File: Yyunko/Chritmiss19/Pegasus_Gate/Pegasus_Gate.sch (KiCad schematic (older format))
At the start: 19 parts, among them U1 WS2811, U2 WS2811, U3 WS2811, U4 WS2811

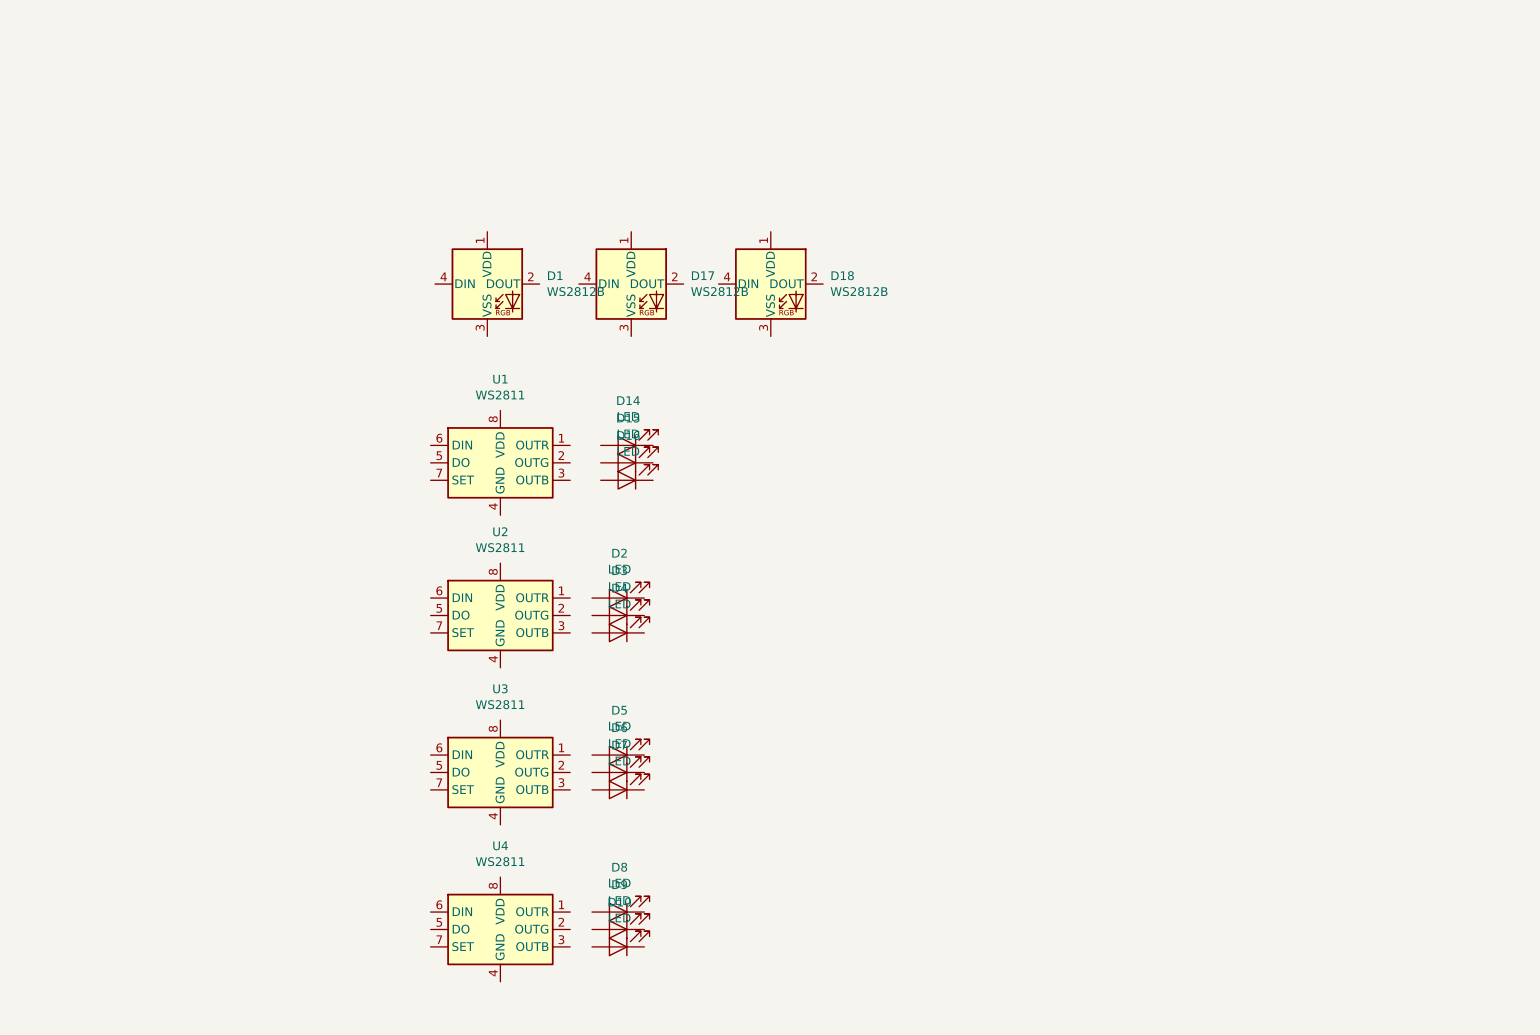
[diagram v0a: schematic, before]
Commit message: Added sidemount LED footprint
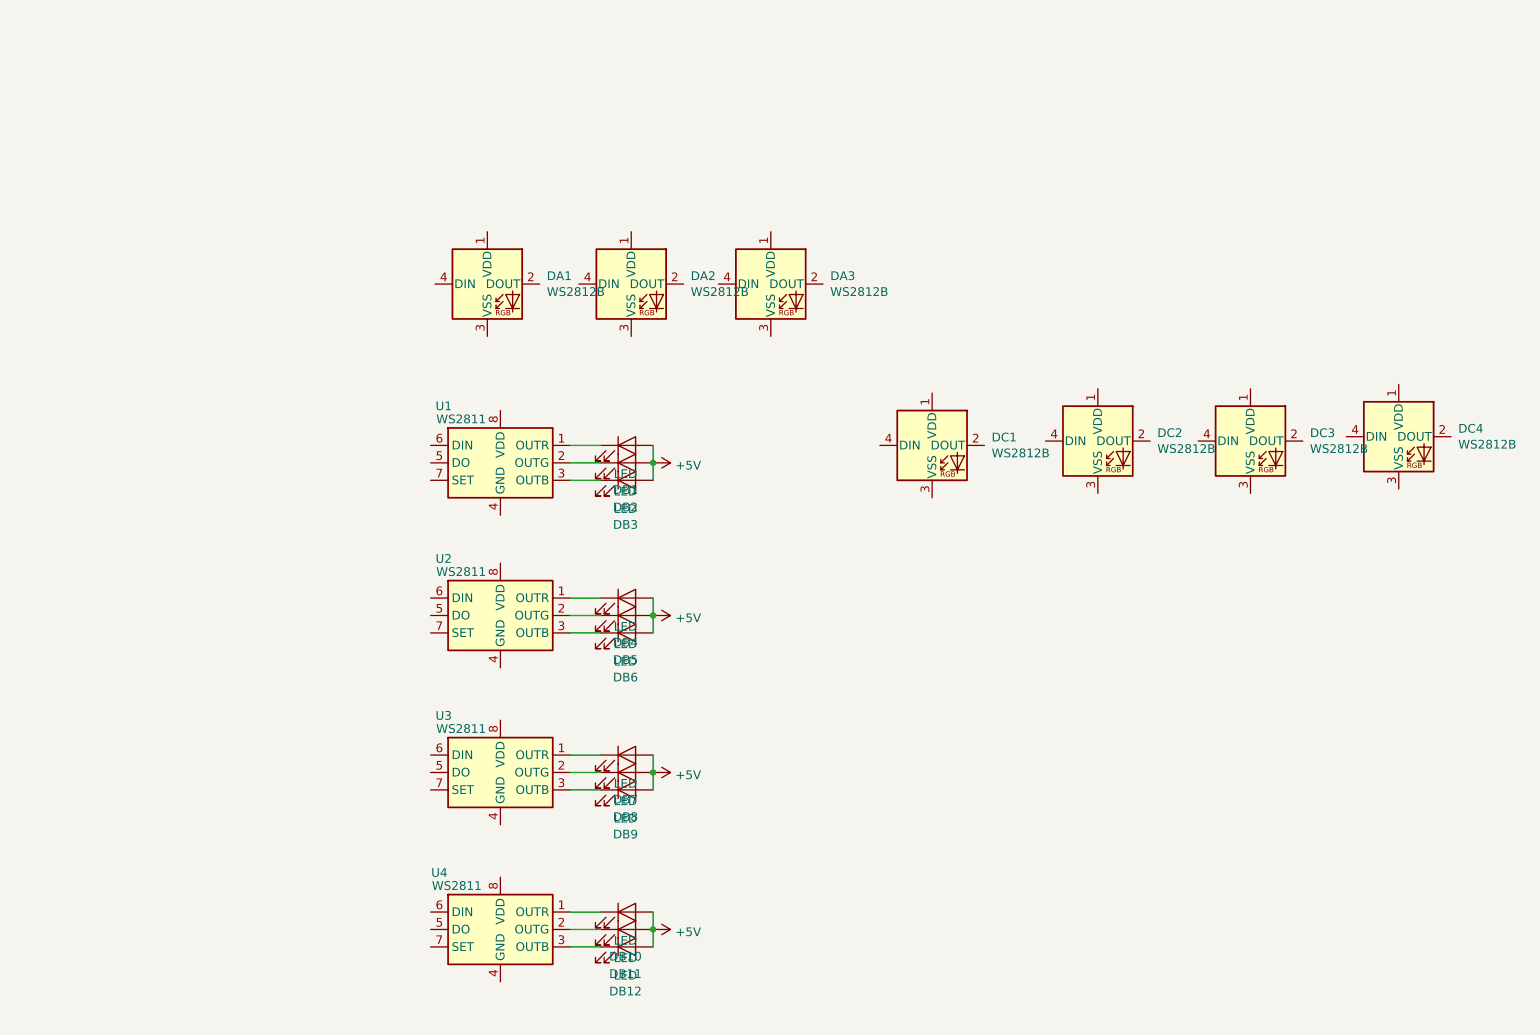
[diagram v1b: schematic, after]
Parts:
- removed D10, D15, D16, D2, D3, D4, D5, D6, D7, D8, D9: LED, LED_SMD:LED_0805_2012Metric_Castellated, symbol Device:LED
- added DB1, DB10, DB11, DB12, DB2, DB4, DB5, DB6, DB7, DB8, DB9: LED, LED_SMD:LED_0805_2012Metric_Castellated, symbol Device:LED
- added DC1, DC2, DC3, DC4: WS2812B, Local:IN-PI42TAS, symbol LED:WS2812B
- U2, U3, U4: footprint (none) -> Package_SO:SSOP-8_3.95x5.21x3.27mm_P1.27mm
- renumbered D1 to DA1, D17 to DA2, D18 to DA3, D14 to DB3
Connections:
- net at U1.1 (OUTR): now also DB1.1 (K)
- net at U1.2 (OUTG): now also DB2.1 (K)
- net at U1.3 (OUTB): now also DB3.1 (K)
- net at U2.1 (OUTR): now also DB4.1 (K)
- net at U2.2 (OUTG): now also DB5.1 (K)
- net at U2.3 (OUTB): now also DB6.1 (K)
- net at U3.1 (OUTR): now also DB7.1 (K)
- net at U3.2 (OUTG): now also DB8.1 (K)
- net at U3.3 (OUTB): now also DB9.1 (K)
- net at U4.1 (OUTR): now also DB10.1 (K)
- net at U4.2 (OUTG): now also DB11.1 (K)
- net at U4.3 (OUTB): now also DB12.1 (K)
- net +5V: now reaches DB3.2 (A)
- net +5V: now also DB1.2 (A), DB10.2 (A), DB11.2 (A), DB12.2 (A), DB2.2 (A), DB4.2 (A), DB5.2 (A), DB6.2 (A), DB7.2 (A), DB8.2 (A), DB9.2 (A)
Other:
- moved on the sheet: DB3

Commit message: Almost sorted all secs out
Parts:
- added C1, C3, C5, C7: 10uF, Capacitor_SMD:C_0805_2012Metric, symbol Device:C
- added C2, C4, C6, C8: 100nF, Capacitor_SMD:C_0805_2012Metric, symbol Device:C_Small
- added DD1, DD2, DD3: WS2812B, Local:IN-PI42TAS, symbol LED:WS2812B
- added J? (x2): Conn_01x03_Female, Connector_PinHeader_2.00mm:PinHeader_1x03_P2.00mm_Vertical, symbol Connector:Conn_01x03_Female
- added JP?: Jumper_NC_Small, Jumper:SolderJumper-2_P1.3mm_Bridged_Pad1.0x1.5mm, symbol Device:Jumper_NC_Small
- renumbered U4 to U1, U3 to U2, U2 to U3, U1 to U4
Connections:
- net +5V: now also DA1.1 (VDD), DA2.1 (VDD), DA3.1 (VDD), U1.8 (VDD), U2.8 (VDD), U3.8 (VDD), U4.8 (VDD), C1.1, C2.1, C3.1, C4.1, C5.1, C6.1, C7.1, C8.1, DD1.1 (VDD), DD2.1 (VDD), DD3.1 (VDD), J?.3 (Pin_3)
- net at DA1.2 (DOUT): now also DD1.4 (DIN)
- net GND: now reaches DA1.3 (VSS)
- net GND: now also DA2.3 (VSS), DA3.3 (VSS), U1.4 (GND), U2.4 (GND), U3.4 (GND), U4.4 (GND), C1.2, C2.2, C3.2, C4.2, C5.2, C6.2, C7.2, C8.2, DD1.3 (VSS), DD2.3 (VSS), DD3.3 (VSS), J?.1 (Pin_1)
- net IN_A: now reaches DA1.4 (DIN)
- net IN_A: now also JP?.2
- net at DA2.2 (DOUT): now also DD2.4 (DIN)
- net at DA2.4 (DIN): now also DD1.2 (DOUT)
- net at DA3.2 (DOUT): now also DD3.4 (DIN)
- net at DA3.4 (DIN): now also DD2.2 (DOUT)
- net IN_C: now reaches U4.5 (DO)
- net IN_C: now also DC1.4 (DIN)
- net at U4.6 (DIN): now also U3.5 (DO)
- net at U3.6 (DIN): now also U2.5 (DO)
- net at U2.6 (DIN): now also U1.5 (DO)
- net IN_B: now reaches U1.6 (DIN)
- net IN_B: now also DD3.2 (DOUT)
- net at DC1.2 (DOUT): now also DC2.4 (DIN)
- net at DC2.2 (DOUT): now also DC3.4 (DIN)
- net at DC3.2 (DOUT): now also DC4.4 (DIN)
- net SIG_OUT: now reaches DC4.2 (DOUT)
- net SIG_OUT: now also J?.2 (Pin_2)
- new net: J?.2 (Pin_2), JP?.1
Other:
- moved on the sheet: DA1, DA2, DA3, DC1, DC2, DC3, DC4

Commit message: Continue woork
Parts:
- gave numbers to parts that had none: 3
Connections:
- net +5V: now also DC1.1 (VDD), DC2.1 (VDD), DC3.1 (VDD), DC4.1 (VDD), J2.1 (Pin_1)
- net GND: now also DC1.3 (VSS), DC2.3 (VSS), DC3.3 (VSS), DC4.3 (VSS), J2.3 (Pin_3)
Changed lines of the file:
@@
 	8750 4475 8925 4475
 $Comp
-L Connector:Conn_01x03_Female J?
+L Connector:Conn_01x03_Female J1
 U 1 1 5DE0950A
 P 3400 2375
-F 0 "J?" H 3294 2050 50  0000 C CNN
+F 0 "J1" H 3294 2050 50  0000 C CNN
 F 1 "Conn_01x03_Female" H 3294 2141 50  0000 C CNN
 F 2 "Connector_PinHeader_2.00mm:PinHeader_1x03_P2.00mm_Vertical" H 3400 2375 50  0001 C CNN
@@
 $EndComp
 $Comp
-L Connector:Conn_01x03_Female J?
+L Connector:Conn_01x03_Female J2
 U 1 1 5DE0969D
 P 10275 2325
-F 0 "J?" H 10169 2000 50  0000 C CNN
+F 0 "J2" H 10169 2000 50  0000 C CNN
 F 1 "Conn_01x03_Female" H 10169 2091 50  0000 C CNN
 F 2 "Connector_PinHeader_2.00mm:PinHeader_1x03_P2.00mm_Vertical" H 10275 2325 50  0001 C CNN
@@
 $EndComp
 $Comp
-L power:GND #PWR?
+L power:GND #PWR0122
 U 1 1 5DE0CA89
 P 3675 2525
-F 0 "#PWR?" H 3675 2275 50  0001 C CNN
+F 0 "#PWR0122" H 3675 2275 50  0001 C CNN
 F 1 "GND" H 3680 2352 50  0000 C CNN
 F 2 "" H 3675 2525 50  0001 C CNN
@@
 	3950 2275 3950 2100
 $Comp
-L power:+5V #PWR?
+L power:+5V #PWR0123
 U 1 1 5DE11560
 P 3950 2100
-F 0 "#PWR?" H 3950 1950 50  0001 C CNN
+F 0 "#PWR0123" H 3950 1950 50  0001 C CNN
 F 1 "+5V" H 3965 2273 50  0000 C CNN
 F 2 "" H 3950 2100 50  0001 C CNN
@@
 $EndComp
 $Comp
-L Device:Jumper_NC_Small JP?
+L Device:Jumper_NC_Small JP1
 U 1 1 5DE11BC5
 P 3750 2375
-F 0 "JP?" H 3750 2587 50  0000 C CNN
+F 0 "JP1" H 3750 2587 50  0000 C CNN
 F 1 "Jumper_NC_Small" H 3750 2496 50  0000 C CNN
 F 2 "Jumper:SolderJumper-2_P1.3mm_Bridged_Pad1.0x1.5mm" H 3750 2375 50  0001 C CNN
@@
 Text Label 10925 2325 2    50   ~ 0
 SIG_OUT
+Wire Wire Line
+	7050 2925 8025 2925
+Wire Wire Line
+	8025 2925 8550 2925
+Connection ~ 8025 2925
+Wire Wire Line
+	9025 2925 10025 2925
+Connection ~ 9025 2925
+Wire Wire Line
+	10025 3525 9025 3525
+Wire Wire Line
+	9025 3525 8550 3525
+Connection ~ 9025 3525
+Wire Wire Line
+	8025 3525 7050 3525
+Connection ~ 8025 3525
+$Comp
+L power:+5V #PWR0124
+U 1 1 5DDFCAF7
+P 8550 2925
+F 0 "#PWR0124" H 8550 2775 50  0001 C CNN
+F 1 "+5V" H 8565 3098 50  0000 C CNN
+F 2 "" H 8550 2925 50  0001 C CNN
+F 3 "" H 8550 2925 50  0001 C CNN
+	1    8550 2925
+	1    0    0    -1
+$EndComp
+Connection ~ 8550 2925
+Wire Wire Line
+	8550 2925 9025 2925
+$Comp
+L power:GND #PWR0125
+U 1 1 5DDFCBC9
+P 8550 3525
+F 0 "#PWR0125" H 8550 3275 50  0001 C CNN
+F 1 "GND" H 8555 3352 50  0000 C CNN
+F 2 "" H 8550 3525 50  0001 C CNN
+F 3 "" H 8550 3525 50  0001 C CNN
+	1    8550 3525
+	1    0    0    -1
+$EndComp
+Connection ~ 8550 3525
+Wire Wire Line
+	8550 3525 8025 3525
+$Comp
+L power:GND #PWR0126
+U 1 1 5DDFD954
+P 10625 2175
+F 0 "#PWR0126" H 10625 1925 50  0001 C CNN
+F 1 "GND" V 10630 2047 50  0000 R CNN
+F 2 "" H 10625 2175 50  0001 C CNN
+F 3 "" H 10625 2175 50  0001 C CNN
+	1    10625 2175
+	0    -1   -1   0
+$EndComp
+$Comp
+L power:+5V #PWR0127
+U 1 1 5DDFDA93
+P 10650 2450
+F 0 "#PWR0127" H 10650 2300 50  0001 C CNN
+F 1 "+5V" V 10665 2578 50  0000 L CNN
+F 2 "" H 10650 2450 50  0001 C CNN
+F 3 "" H 10650 2450 50  0001 C CNN
+	1    10650 2450
+	0    1    1    0
+$EndComp
+Wire Wire Line
+	10475 2425 10650 2425
+Wire Wire Line
+	10650 2425 10650 2450
+Wire Wire Line
+	10475 2225 10625 2225
+Wire Wire Line
+	10625 2225 10625 2175
 $EndSCHEMATC

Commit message: Begin work on assigning part nums
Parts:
- DA1, DA2, DA3: value WS2812B -> BL-HRGB32K-3-TRBCT-ND
- DB1, DB10, DB11, DB12, DB2, DB3, DB4, DB5, DB6, DB7, DB8, DB9: value LED -> 754-1437-6-ND
- DC1, DC2, DC3, DC4, DD1, DD2, DD3: value WS2812B -> 1830-1206-1-ND
- U4: value WS2811 -> 1528-1537-ND
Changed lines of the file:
@@
 P 5075 1550
 F 0 "DA1" H 5416 1596 50  0000 L CNN
-F 1 "WS2812B" H 5416 1505 50  0000 L CNN
+F 1 "BL-HRGB32K-3-TRBCT-ND" H 5416 1505 50  0000 L CNN
 F 2 "LED_SMD:LED_WS2812B_PLCC4_5.0x5.0mm_P3.2mm" H 5125 1250 50  0001 L TNN
 F 3 "https://cdn-shop.adafruit.com/datasheets/WS2812B.pdf" H 5175 1175 50  0001 L TNN
@@
 P 6400 1675
 F 0 "DA2" H 6741 1721 50  0000 L CNN
-F 1 "WS2812B" H 6741 1630 50  0000 L CNN
+F 1 "BL-HRGB32K-3-TRBCT-ND" H 6741 1630 50  0000 L CNN
 F 2 "LED_SMD:LED_WS2812B_PLCC4_5.0x5.0mm_P3.2mm" H 6450 1375 50  0001 L TNN
 F 3 "https://cdn-shop.adafruit.com/datasheets/WS2812B.pdf" H 6500 1300 50  0001 L TNN
@@
 P 7750 1550
 F 0 "DA3" H 8091 1596 50  0000 L CNN
-F 1 "WS2812B" H 8091 1505 50  0000 L CNN
+F 1 "BL-HRGB32K-3-TRBCT-ND" H 8091 1505 50  0000 L CNN
 F 2 "LED_SMD:LED_WS2812B_PLCC4_5.0x5.0mm_P3.2mm" H 7800 1250 50  0001 L TNN
 F 3 "https://cdn-shop.adafruit.com/datasheets/WS2812B.pdf" H 7850 1175 50  0001 L TNN
@@
 P 5375 3600
 F 0 "U4" H 5050 3925 50  0000 C CNN
-F 1 "WS2811" H 5150 3850 50  0000 C CNN
+F 1 "1528-1537-ND" H 5150 3850 50  0000 C CNN
 F 2 "Package_SO:SSOP-8_3.95x5.21x3.27mm_P1.27mm" H 5075 3750 50  0001 C CNN
 F 3 "https://cdn-shop.adafruit.com/datasheets/WS2811.pdf" H 5175 3850 50  0001 C CNN
@@
 P 6100 3700
 F 0 "DB3" H 6092 3445 50  0000 C CNN
-F 1 "LED" H 6092 3536 50  0000 C CNN
+F 1 "754-1437-6-ND" H 6092 3536 50  0000 C CNN
 F 2 "LED_SMD:LED_0805_2012Metric_Castellated" H 6100 3700 50  0001 C CNN
 F 3 "~" H 6100 3700 50  0001 C CNN
@@
 P 6100 3600
 F 0 "DB2" H 6092 3345 50  0000 C CNN
-F 1 "LED" H 6092 3436 50  0000 C CNN
+F 1 "754-1437-6-ND" H 6092 3436 50  0000 C CNN
 F 2 "LED_SMD:LED_0805_2012Metric_Castellated" H 6100 3600 50  0001 C CNN
 F 3 "~" H 6100 3600 50  0001 C CNN
@@
 P 6100 3500
 F 0 "DB1" H 6092 3245 50  0000 C CNN
-F 1 "LED" H 6092 3336 50  0000 C CNN
+F 1 "754-1437-6-ND" H 6092 3336 50  0000 C CNN
 F 2 "LED_SMD:LED_0805_2012Metric_Castellated" H 6100 3500 50  0001 C CNN
 F 3 "~" H 6100 3500 50  0001 C CNN
@@
 P 6100 4575
 F 0 "DB6" H 6092 4320 50  0000 C CNN
-F 1 "LED" H 6092 4411 50  0000 C CNN
+F 1 "754-1437-6-ND" H 6092 4411 50  0000 C CNN
 F 2 "LED_SMD:LED_0805_2012Metric_Castellated" H 6100 4575 50  0001 C CNN
 F 3 "~" H 6100 4575 50  0001 C CNN
@@
 P 6100 4475
 F 0 "DB5" H 6092 4220 50  0000 C CNN
-F 1 "LED" H 6092 4311 50  0000 C CNN
+F 1 "754-1437-6-ND" H 6092 4311 50  0000 C CNN
 F 2 "LED_SMD:LED_0805_2012Metric_Castellated" H 6100 4475 50  0001 C CNN
 F 3 "~" H 6100 4475 50  0001 C CNN
@@
 P 6100 4375
 F 0 "DB4" H 6092 4120 50  0000 C CNN
-F 1 "LED" H 6092 4211 50  0000 C CNN
+F 1 "754-1437-6-ND" H 6092 4211 50  0000 C CNN
 F 2 "LED_SMD:LED_0805_2012Metric_Castellated" H 6100 4375 50  0001 C CNN
 F 3 "~" H 6100 4375 50  0001 C CNN
@@
 P 6100 5475
 F 0 "DB9" H 6092 5220 50  0000 C CNN
-F 1 "LED" H 6092 5311 50  0000 C CNN
+F 1 "754-1437-6-ND" H 6092 5311 50  0000 C CNN
 F 2 "LED_SMD:LED_0805_2012Metric_Castellated" H 6100 5475 50  0001 C CNN
 F 3 "~" H 6100 5475 50  0001 C CNN
@@
 P 6100 5375
 F 0 "DB8" H 6092 5120 50  0000 C CNN
-F 1 "LED" H 6092 5211 50  0000 C CNN
+F 1 "754-1437-6-ND" H 6092 5211 50  0000 C CNN
 F 2 "LED_SMD:LED_0805_2012Metric_Castellated" H 6100 5375 50  0001 C CNN
 F 3 "~" H 6100 5375 50  0001 C CNN
@@
 P 6100 5275
 F 0 "DB7" H 6092 5020 50  0000 C CNN
-F 1 "LED" H 6092 5111 50  0000 C CNN
+F 1 "754-1437-6-ND" H 6092 5111 50  0000 C CNN
 F 2 "LED_SMD:LED_0805_2012Metric_Castellated" H 6100 5275 50  0001 C CNN
 F 3 "~" H 6100 5275 50  0001 C CNN
@@
 P 6100 6375
 F 0 "DB12" H 6092 6120 50  0000 C CNN
-F 1 "LED" H 6092 6211 50  0000 C CNN
+F 1 "754-1437-6-ND" H 6092 6211 50  0000 C CNN
 F 2 "LED_SMD:LED_0805_2012Metric_Castellated" H 6100 6375 50  0001 C CNN
 F 3 "~" H 6100 6375 50  0001 C CNN
@@
 P 6100 6275
 F 0 "DB11" H 6092 6020 50  0000 C CNN
-F 1 "LED" H 6092 6111 50  0000 C CNN
+F 1 "754-1437-6-ND" H 6092 6111 50  0000 C CNN
 F 2 "LED_SMD:LED_0805_2012Metric_Castellated" H 6100 6275 50  0001 C CNN
 F 3 "~" H 6100 6275 50  0001 C CNN
@@
 P 6100 6175
 F 0 "DB10" H 6092 5920 50  0000 C CNN
-F 1 "LED" H 6092 6011 50  0000 C CNN
+F 1 "754-1437-6-ND" H 6092 6011 50  0000 C CNN
 F 2 "LED_SMD:LED_0805_2012Metric_Castellated" H 6100 6175 50  0001 C CNN
 F 3 "~" H 6100 6175 50  0001 C CNN
@@
 P 7050 3225
 F 0 "DC1" H 7391 3271 50  0000 L CNN
-F 1 "WS2812B" H 7391 3180 50  0000 L CNN
+F 1 "1830-1206-1-ND" H 7391 3180 50  0000 L CNN
 F 2 "Local:IN-PI42TAS" H 7100 2925 50  0001 L TNN
 F 3 "https://cdn-shop.adafruit.com/datasheets/WS2812B.pdf" H 7150 2850 50  0001 L TNN
@@
 P 8025 3225
 F 0 "DC2" H 8366 3271 50  0000 L CNN
-F 1 "WS2812B" H 8366 3180 50  0000 L CNN
+F 1 "1830-1206-1-ND" H 8366 3180 50  0000 L CNN
 F 2 "Local:IN-PI42TAS" H 8075 2925 50  0001 L TNN
 F 3 "https://cdn-shop.adafruit.com/datasheets/WS2812B.pdf" H 8125 2850 50  0001 L TNN
@@
 P 9025 3225
 F 0 "DC3" H 9366 3271 50  0000 L CNN
-F 1 "WS2812B" H 9366 3180 50  0000 L CNN
+F 1 "1830-1206-1-ND" H 9366 3180 50  0000 L CNN
 F 2 "Local:IN-PI42TAS" H 9075 2925 50  0001 L TNN
 F 3 "https://cdn-shop.adafruit.com/datasheets/WS2812B.pdf" H 9125 2850 50  0001 L TNN
@@
 P 10025 3225
 F 0 "DC4" H 10366 3271 50  0000 L CNN
-F 1 "WS2812B" H 10366 3180 50  0000 L CNN
+F 1 "1830-1206-1-ND" H 10366 3180 50  0000 L CNN
 F 2 "Local:IN-PI42TAS" H 10075 2925 50  0001 L TNN
 F 3 "https://cdn-shop.adafruit.com/datasheets/WS2812B.pdf" H 10125 2850 50  0001 L TNN
@@
 P 5800 1550
 F 0 "DD1" H 6141 1596 50  0000 L CNN
-F 1 "WS2812B" H 6141 1505 50  0000 L CNN
+F 1 "1830-1206-1-ND" H 6141 1505 50  0000 L CNN
 F 2 "Local:IN-PI42TAS" H 5850 1250 50  0001 L TNN
 F 3 "https://cdn-shop.adafruit.com/datasheets/WS2812B.pdf" H 5900 1175 50  0001 L TNN
@@
 P 8475 1550
 F 0 "DD3" H 8816 1596 50  0000 L CNN
-F 1 "WS2812B" H 8816 1505 50  0000 L CNN
+F 1 "1830-1206-1-ND" H 8816 1505 50  0000 L CNN
 F 2 "Local:IN-PI42TAS" H 8525 1250 50  0001 L TNN
 F 3 "https://cdn-shop.adafruit.com/datasheets/WS2812B.pdf" H 8575 1175 50  0001 L TNN
@@
 P 7150 1675
 F 0 "DD2" H 7491 1721 50  0000 L CNN
-F 1 "WS2812B" H 7491 1630 50  0000 L CNN
+F 1 "1830-1206-1-ND" H 7491 1630 50  0000 L CNN
 F 2 "Local:IN-PI42TAS" H 7200 1375 50  0001 L TNN
 F 3 "https://cdn-shop.adafruit.com/datasheets/WS2812B.pdf" H 7250 1300 50  0001 L TNN

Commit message: Continue work on durg ring thing
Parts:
- added SYM1: SYM_Radioactive_Large, Local:DragonIcon, symbol Graphic:SYM_Radioactive_Large
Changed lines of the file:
@@
 Wire Wire Line
 	10625 2225 10625 2175
+$Comp
+L Graphic:SYM_Radioactive_Large SYM1
+U 1 1 5DE0498B
+P 2700 6025
+F 0 "SYM1" H 2795 6305 50  0001 C CNN
+F 1 "SYM_Radioactive_Large" H 2795 5855 50  0001 C CNN
+F 2 "Local:DragonIcon" H 2795 5905 50  0001 C CNN
+F 3 "~" H 2825 5905 50  0001 C CNN
+	1    2700 6025
+	1    0    0    -1
+$EndComp
 $EndSCHEMATC
